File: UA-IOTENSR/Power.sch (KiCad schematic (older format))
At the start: 28 parts, among them IC201 BQ2000TPN-B5, J201 ZX62-AB-5PA_31_, U2 AP63203WU

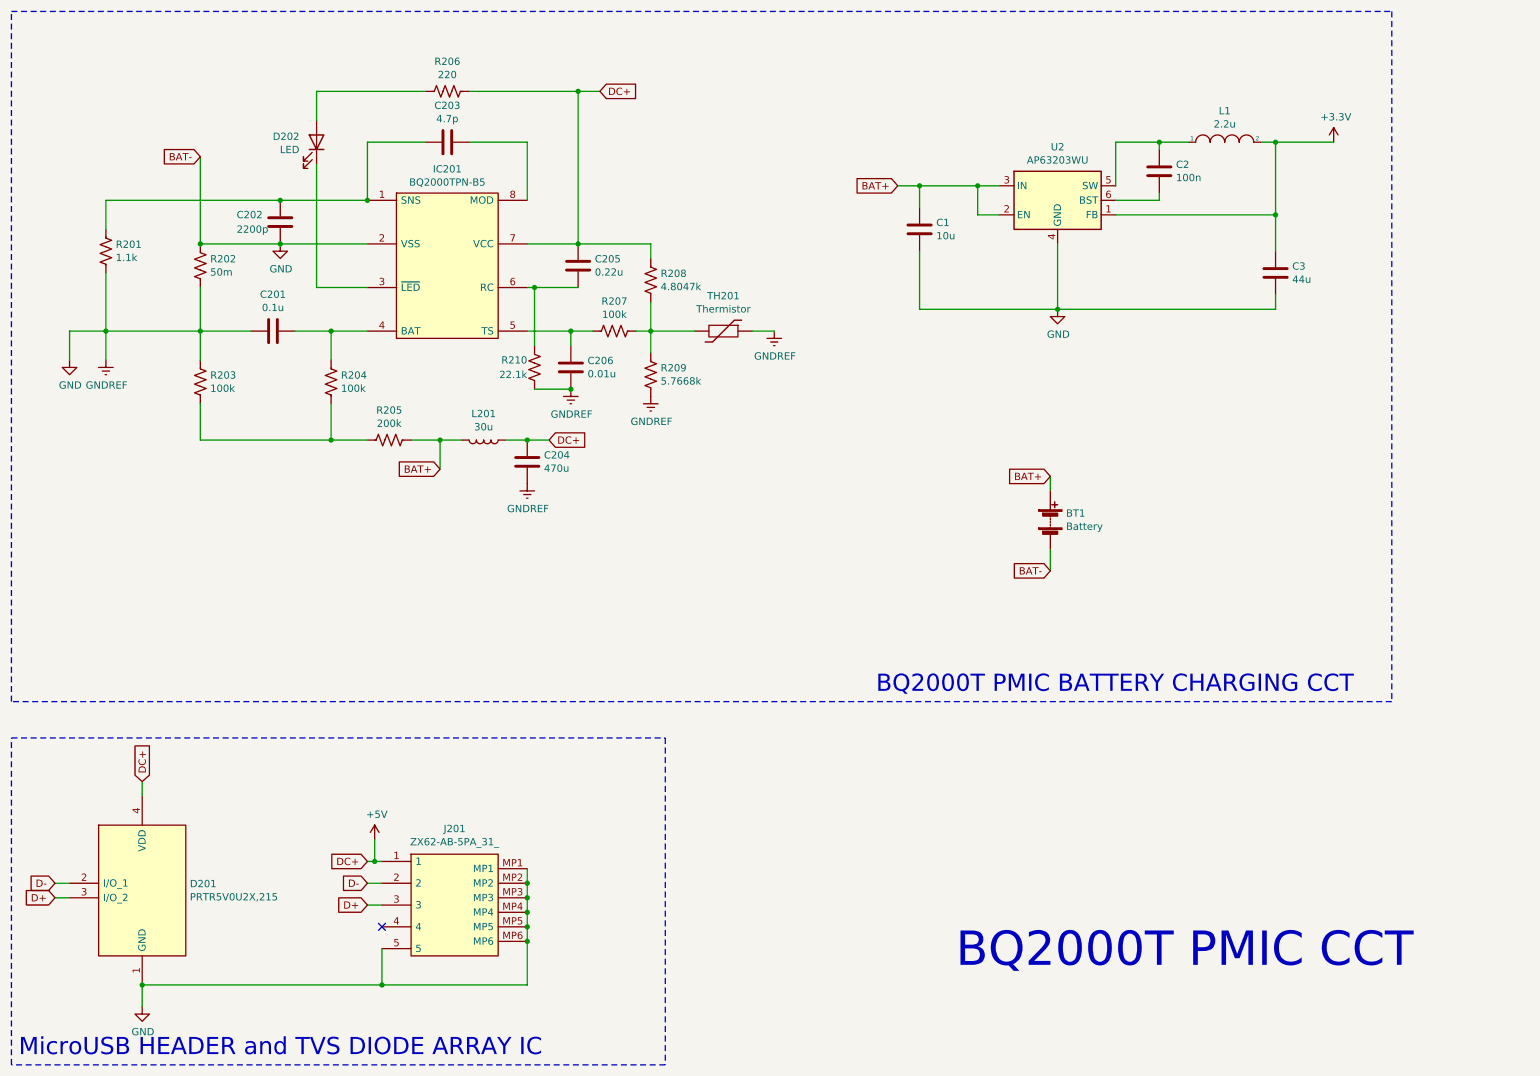
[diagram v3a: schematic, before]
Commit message: Re-annotated schem, progress on layout
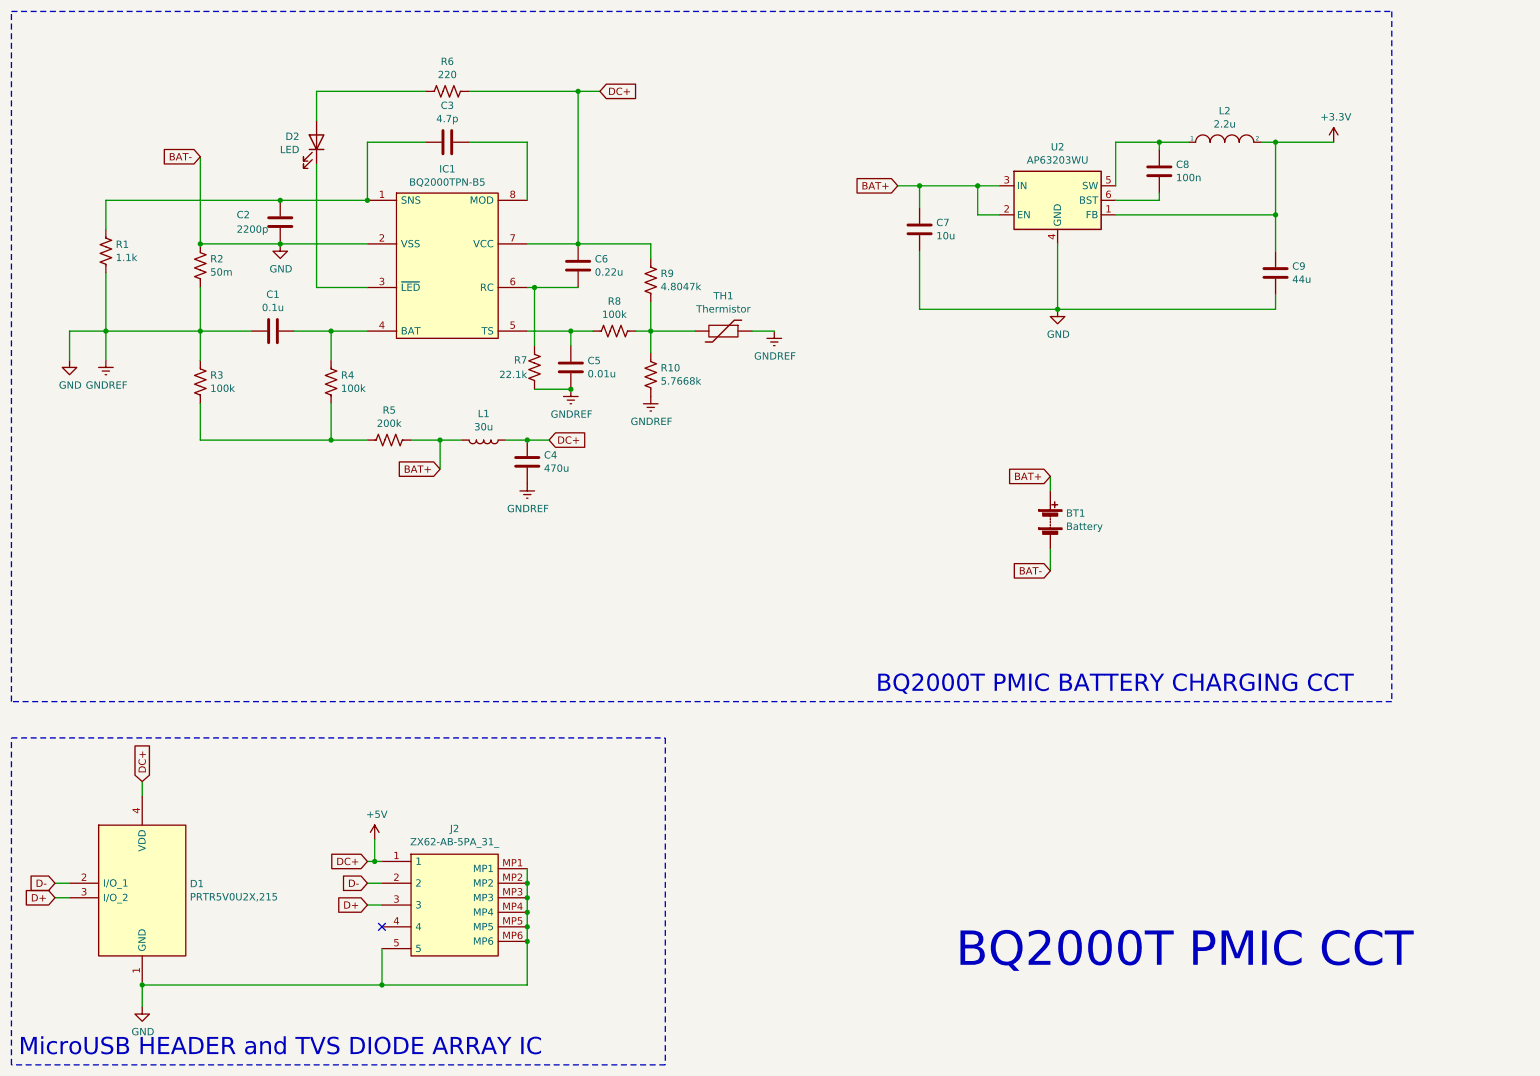
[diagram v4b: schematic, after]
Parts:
- renumbered C201 to C1, C202 to C2, C203 to C3, C204 to C4, C206 to C5, C205 to C6, C1 to C7, C2 to C8, C3 to C9, D201 to D1, D202 to D2, IC201 to IC1, J201 to J2, L201 to L1, L1 to L2, R201 to R1, R209 to R10, R202 to R2, R203 to R3, R204 to R4, R205 to R5, R206 to R6, R210 to R7, R207 to R8, R208 to R9, TH201 to TH1

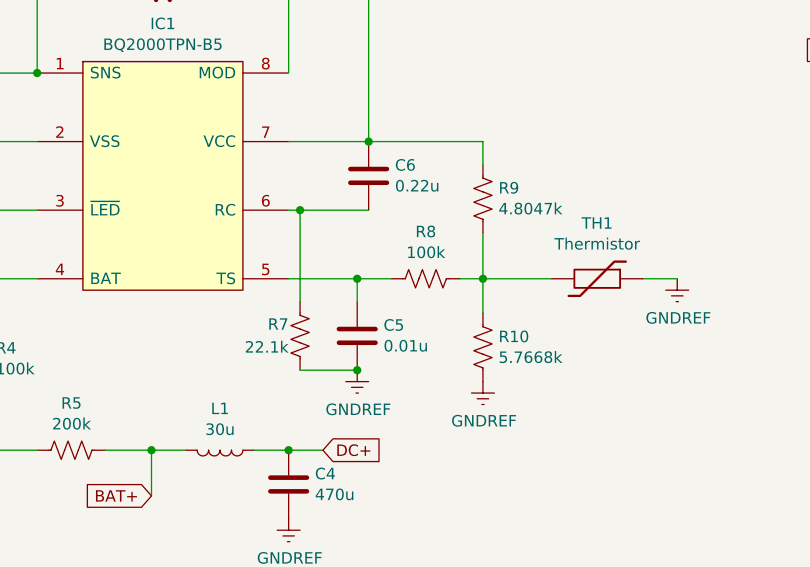
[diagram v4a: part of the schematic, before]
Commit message: Updated resistor values within the schematic
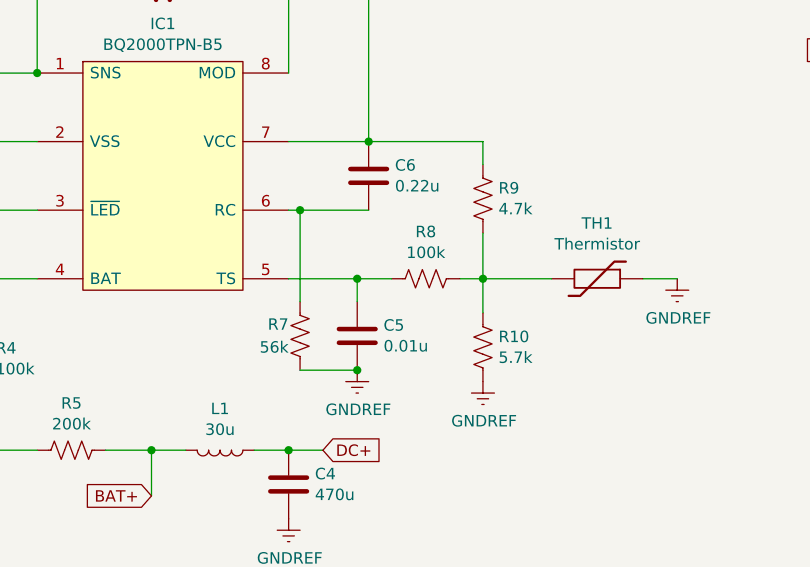
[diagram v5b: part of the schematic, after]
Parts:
- R10: value 5.7668k -> 5.7k
- R7: value 22.1k -> 56k
- R9: value 4.8047k -> 4.7k
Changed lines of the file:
@@
 P 4100 2950
 F 0 "R7" H 4150 2900 50  0000 L CNN
-F 1 "22.1k" H 4150 3000 50  0000 L CNN
+F 1 "56k" H 4150 3000 50  0000 L CNN
 F 2 "RNCP0805FTD22K1:RESC2012X60N" V 4140 2940 50  0001 C CNN
 F 3 "~" H 4100 2950 50  0001 C CNN
@@
 P 4900 3000
 F 0 "R10" H 4968 3046 50  0000 L CNN
-F 1 "5.7668k" H 4968 2955 50  0000 L CNN
+F 1 "5.7k" H 4968 2955 50  0000 L CNN
 F 2 "Resistor_SMD:R_0805_2012Metric_Pad1.20x1.40mm_HandSolder" V 4940 2990 50  0001 C CNN
 F 3 "~" H 4900 3000 50  0001 C CNN
@@
 P 4900 2350
 F 0 "R9" H 4968 2396 50  0000 L CNN
-F 1 "4.8047k" H 4968 2305 50  0000 L CNN
+F 1 "4.7k" H 4968 2305 50  0000 L CNN
 F 2 "Resistor_SMD:R_0805_2012Metric_Pad1.20x1.40mm_HandSolder" V 4940 2340 50  0001 C CNN
 F 3 "~" H 4900 2350 50  0001 C CNN

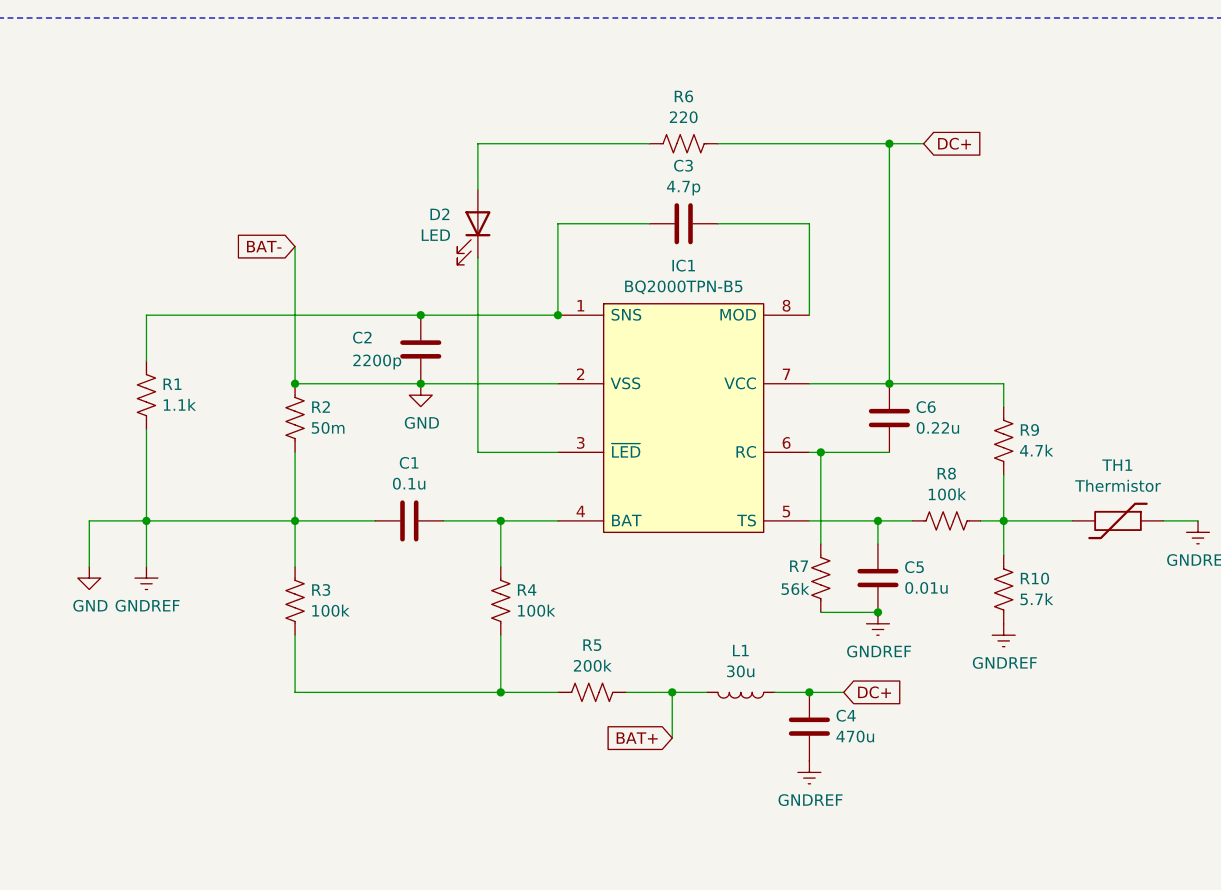
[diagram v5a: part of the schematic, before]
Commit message: Component labels and values updated
Re labelled components to match the hand drawn schematic.
Updated component values to reflect the redesign.
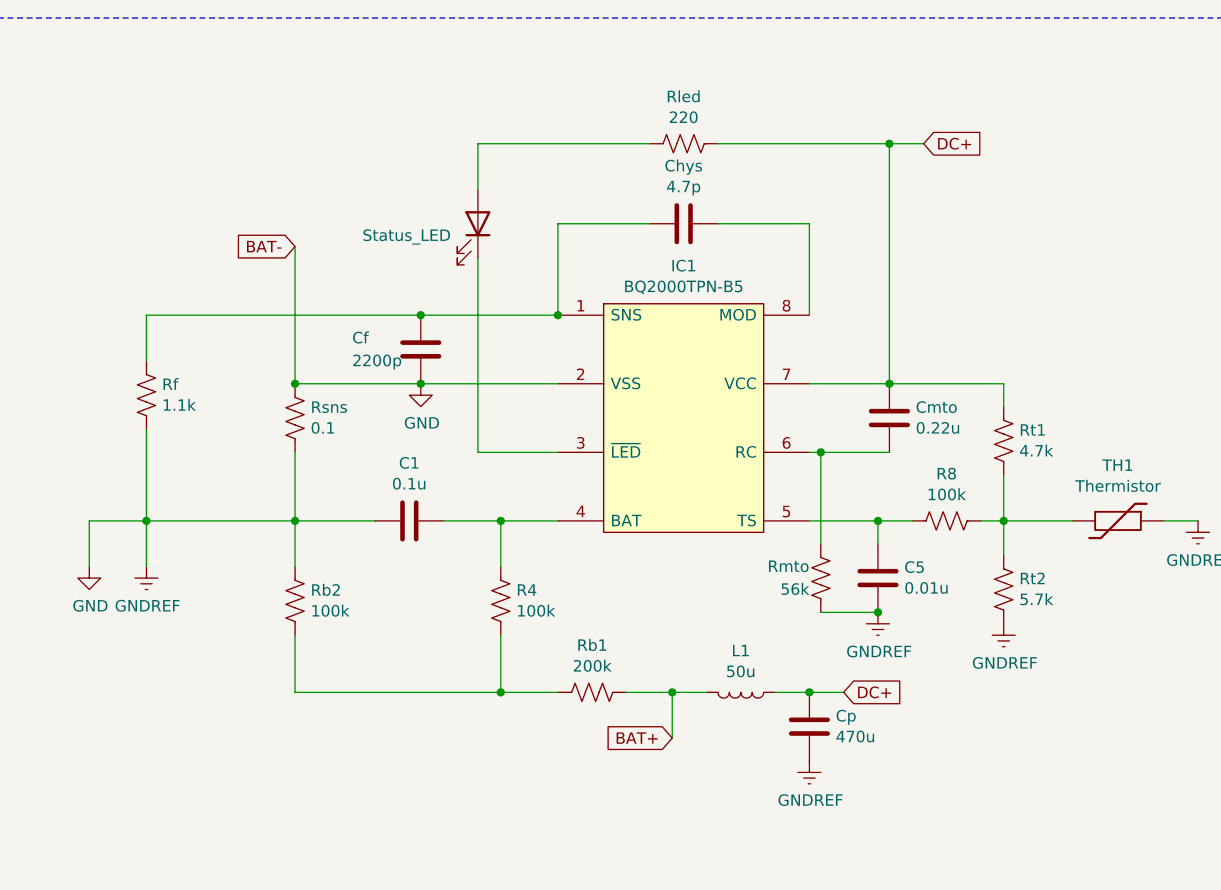
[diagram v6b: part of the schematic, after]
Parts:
- D2: value LED -> Status_LED
- L1: value 30u -> 50u
- Rsns: renamed from R2; value 50m -> 0.1
- renumbered C2 to Cf, C3 to Chys, C6 to Cmto, C4 to Cp, R5 to Rb1, R3 to Rb2, R1 to Rf, R6 to Rled, R7 to Rmto, R9 to Rt1, R10 to Rt2
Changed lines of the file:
@@
 $Descr A4 11693 8268
 encoding utf-8
-Sheet 2 2
+Sheet 1 1
 Title ""
 Date ""
@@
 $EndComp
 $Comp
-L Device:C C3
+L Device:C Chys
 U 1 1 61E48DB8
 P 3500 1400
-F 0 "C3" V 3248 1400 50  0000 C CNN
+F 0 "Chys" V 3248 1400 50  0000 C CNN
 F 1 "4.7p" V 3339 1400 50  0000 C CNN
 F 2 "Capacitor_SMD:C_0805_2012Metric" H 3538 1250 50  0001 C CNN
@@
 	3650 1400 4050 1400
 $Comp
-L Device:C C6
+L Device:C Cmto
 U 1 1 61E4BE8D
 P 4400 2250
-F 0 "C6" H 4515 2296 50  0000 L CNN
+F 0 "Cmto" H 4515 2296 50  0000 L CNN
 F 1 "0.22u" H 4515 2205 50  0000 L CNN
 F 2 "Capacitor_SMD:C_0805_2012Metric" H 4438 2100 50  0001 C CNN
@@
 	1150 1800 1150 2000
 $Comp
-L Device:R_US R1
+L Device:R_US Rf
 U 1 1 61E4F5EE
 P 1150 2150
-F 0 "R1" H 1218 2196 50  0000 L CNN
+F 0 "Rf" H 1218 2196 50  0000 L CNN
 F 1 "1.1k" H 1218 2105 50  0000 L CNN
 F 2 "SamacSys_Parts:ERA8A__0805_" V 1190 2140 50  0001 C CNN
@@
 	1800 2100 1800 1500
 $Comp
-L Device:R_US R2
+L Device:R_US Rsns
 U 1 1 61E54493
 P 1800 2250
-F 0 "R2" H 1868 2296 50  0000 L CNN
-F 1 "50m" H 1868 2205 50  0000 L CNN
+F 0 "Rsns" H 1868 2296 50  0000 L CNN
+F 1 "0.1" H 1868 2205 50  0000 L CNN
 F 2 "SamacSys_Parts:RESC6331X80N" V 1840 2240 50  0001 C CNN
 F 3 "~" H 1800 2250 50  0001 C CNN
@@
 Connection ~ 1800 2100
 $Comp
-L Device:C C2
+L Device:C Cf
 U 1 1 61E55DC2
 P 2350 1950
-F 0 "C2" H 2050 2000 50  0000 L CNN
+F 0 "Cf" H 2050 2000 50  0000 L CNN
 F 1 "2200p" H 2050 1900 50  0000 L CNN
 F 2 "Capacitor_SMD:C_0805_2012Metric" H 2388 1800 50  0001 C CNN
@@
 	1150 2700 1150 2900
 $Comp
-L Device:R_US R3
+L Device:R_US Rb2
 U 1 1 61E58746
 P 1800 3050
-F 0 "R3" H 1868 3096 50  0000 L CNN
+F 0 "Rb2" H 1868 3096 50  0000 L CNN
 F 1 "100k" H 1868 3005 50  0000 L CNN
 F 2 "SamacSys_Parts:RESC5025X70N" V 1840 3040 50  0001 C CNN
@@
 Connection ~ 2700 3450
 $Comp
-L Device:R_US R5
+L Device:R_US Rb1
 U 1 1 61E5C7B1
 P 3100 3450
-F 0 "R5" V 2895 3450 50  0000 C CNN
+F 0 "Rb1" V 2895 3450 50  0000 C CNN
 F 1 "200k" V 2986 3450 50  0000 C CNN
 F 2 "SamacSys_Parts:RESC1608X55N" V 3140 3440 50  0001 C CNN
@@
 U 1 1 61E5EE17
 P 2600 1400
-F 0 "D2" V 2639 1282 50  0000 R CNN
-F 1 "LED" V 2548 1282 50  0000 R CNN
+F 0 "D2" V 2639 1282 50  0001 R CNN
+F 1 "Status_LED" V 2548 1282 50  0000 R CNN
 F 2 "LED_SMD:LED_1206_3216Metric" H 2600 1400 50  0001 C CNN
 F 3 "~" H 2600 1400 50  0001 C CNN
@@
 	2600 1550 2600 2400
 $Comp
-L Device:R_US R6
+L Device:R_US Rled
 U 1 1 61E65328
 P 3500 1050
-F 0 "R6" V 3295 1050 50  0000 C CNN
+F 0 "Rled" V 3295 1050 50  0000 C CNN
 F 1 "220" V 3386 1050 50  0000 C CNN
 F 2 "SamacSys_Parts:RESC3116X65N" V 3540 1040 50  0001 C CNN
@@
 P 3750 3450
 F 0 "L1" V 3569 3450 50  0000 C CNN
-F 1 "30u" V 3660 3450 50  0000 C CNN
+F 1 "50u" V 3660 3450 50  0000 C CNN
 F 2 "Inductor_SMD:L_0805_2012Metric_Pad1.15x1.40mm_HandSolder" H 3750 3450 50  0001 C CNN
 F 3 "~" H 3750 3450 50  0001 C CNN
@@
 	3900 3450 4050 3450
 $Comp
-L Device:C C4
+L Device:C Cp
 U 1 1 61E6B59F
 P 4050 3600
-F 0 "C4" H 4165 3646 50  0000 L CNN
+F 0 "Cp" H 4165 3646 50  0000 L CNN
 F 1 "470u" H 4165 3555 50  0000 L CNN
 F 2 "Capacitor_SMD:C_0805_2012Metric" H 4088 3450 50  0001 C CNN
@@
 BAT+
 $Comp
-L Device:R_US R7
+L Device:R_US Rmto
 U 1 1 61E84528
 P 4100 2950
-F 0 "R7" H 4150 2900 50  0000 L CNN
+F 0 "Rmto" H 4150 2900 50  0000 L CNN
 F 1 "56k" H 4150 3000 50  0000 L CNN
 F 2 "RNCP0805FTD22K1:RESC2012X60N" V 4140 2940 50  0001 C CNN
@@
 	4900 2200 4900 2100
 $Comp
-L Device:R_US R10
+L Device:R_US Rt2
 U 1 1 6209F5C7
 P 4900 3000
-F 0 "R10" H 4968 3046 50  0000 L CNN
+F 0 "Rt2" H 4968 3046 50  0000 L CNN
 F 1 "5.7k" H 4968 2955 50  0000 L CNN
 F 2 "Resistor_SMD:R_0805_2012Metric_Pad1.20x1.40mm_HandSolder" V 4940 2990 50  0001 C CNN
@@
 $EndComp
 $Comp
-L Device:R_US R9
+L Device:R_US Rt1
 U 1 1 620A85C3
 P 4900 2350
-F 0 "R9" H 4968 2396 50  0000 L CNN
+F 0 "Rt1" H 4968 2396 50  0000 L CNN
 F 1 "4.7k" H 4968 2305 50  0000 L CNN
 F 2 "Resistor_SMD:R_0805_2012Metric_Pad1.20x1.40mm_HandSolder" V 4940 2340 50  0001 C CNN

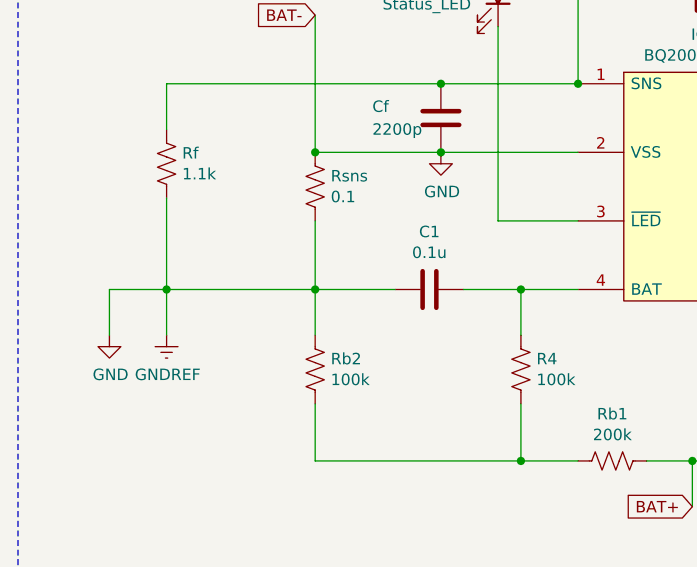
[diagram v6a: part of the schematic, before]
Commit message: Isolated GNDS and label updates
Updated GND labels
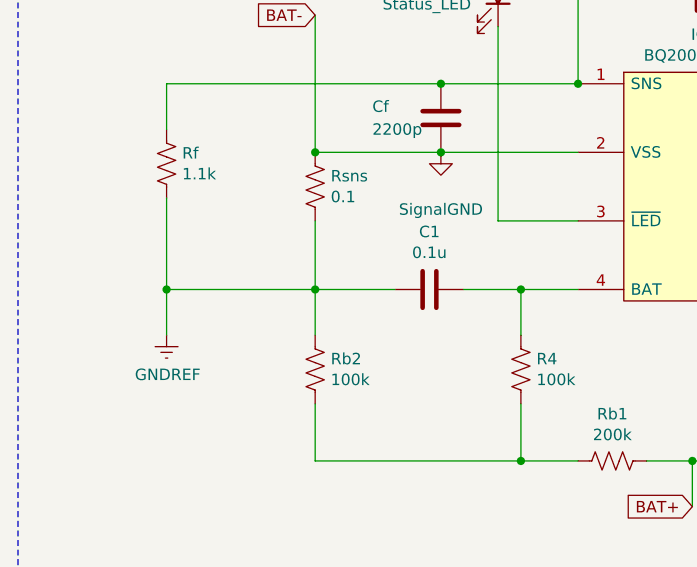
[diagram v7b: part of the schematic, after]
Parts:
- added SignalGND: GND, symbol power:GND
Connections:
- net GND: now also SignalGND.1 (GND); no longer C1.2, C5.2, Cp.2, Rb2.1, Rf.2, Rmto.1, Rsns.2, Rt2.2, TH1.1
- new net GNDREF: C1.2, C5.2, Cp.2, Rb2.1, Rf.2, Rmto.1, Rsns.2, Rt2.2, TH1.1
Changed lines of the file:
@@
 	2350 2100 2950 2100
 $Comp
-L power:GND #PWR09
+L power:GND SignalGND
 U 1 1 61E56BD7
 P 2350 2100
-F 0 "#PWR09" H 2350 1850 50  0001 C CNN
-F 1 "GND" H 2355 1927 50  0000 C CNN
+F 0 "SignalGND" H 2350 1850 50  0000 C CNN
+F 1 "GND" H 2355 1927 50  0001 C CNN
 F 2 "" H 2350 2100 50  0001 C CNN
 F 3 "" H 2350 2100 50  0001 C CNN
@@
 DC+
 NoConn ~ 3050 6800
-$Comp
-L power:GND #PWR06
-U 1 1 620A89C0
-P 900 2900
-F 0 "#PWR06" H 900 2650 50  0001 C CNN
-F 1 "GND" H 905 2727 50  0000 C CNN
-F 2 "" H 900 2900 50  0001 C CNN
-F 3 "" H 900 2900 50  0001 C CNN
-	1    900  2900
-	1    0    0    -1
-$EndComp
-Wire Wire Line
-	900  2700 900  2900
-Wire Wire Line
-	900  2700 1150 2700
 Wire Wire Line
 	4900 2100 4400 2100
